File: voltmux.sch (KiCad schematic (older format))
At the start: 32 parts, among them J5 Conn_02x07_Odd_Even, U10 CD74HC4067SM

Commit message: Updated all the caps (I think) mostly changed to 0805
- Added 0603 footprints to new resistors which is slightly different from the old 0603 resistors for some reason???
- Annotated the schematic
- Still need to do the inductor oof
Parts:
- C13: footprint Capacitor_SMD:C_1206_3216Metric -> Capacitor_SMD:C_0805_2012Metric; Comment (none) -> 0.1µF -20%, +80% 16V Ceramic Capacitor Y5V 0805 (2012 Metri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; Digikey Number (none) -> 399-9159-2-ND; Part Number (none) -> C0805C104Z4VACTU; Price ($) (none) -> 0.11
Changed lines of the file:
@@
 	2350 3550 2350 3500
-$Comp
-L Device:C_Small C13
-U 1 1 5F5548EC
-P 2500 1250
-F 0 "C13" H 2592 1296 50  0000 L CNN
-F 1 "0.1uF" H 2592 1205 50  0000 L CNN
-F 2 "Capacitor_SMD:C_1206_3216Metric" H 2500 1250 50  0001 C CNN
-F 3 "~" H 2500 1250 50  0001 C CNN
-	1    2500 1250
-	1    0    0    -1
-$EndComp
 $Comp
 L power:GND #PWR046
@@
 	10450 2100 10400 2100
 NoConn ~ 10450 2700
+$Comp
+L Device:C_Small C?
+U 1 1 5FD72535
+P 2500 1250
+AR Path="/5FD72535" Ref="C?"  Part="1"
+AR Path="/5F70A721/5FD72535" Ref="C13"  Part="1"
+F 0 "C13" H 2592 1296 50  0000 L CNN
+F 1 "0.1uF" H 2592 1205 50  0000 L CNN
+F 2 "Capacitor_SMD:C_0805_2012Metric" H 2500 1250 50  0001 C CNN
+F 3 "https://content.kemet.com/datasheets/KEM_C1005_Y5V_SMD.pdf" H 2500 1250 50  0001 C CNN
+F 4 "C0805C104Z4VACTU" H 2500 1250 50  0001 C CNN "Part Number"
+F 5 "399-9159-2-ND" H 2500 1250 50  0001 C CNN "Digikey Number"
+F 6 "0.11" H 2500 1250 50  0001 C CNN "Price ($)"
+F 7 "0.1µF -20%, +80% 16V Ceramic Capacitor Y5V 0805 (2012 Metric)" H 2500 1250 50  0001 C CNN "Comment"
+	1    2500 1250
+	1    0    0    -1
+$EndComp
 $EndSCHEMATC

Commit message: Reset 0604 resistors to smaller (older?) footprint size
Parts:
- R31, R32, R33, R34, R35, R36, R37, R38, R39, R40, R41, R42, R43, R44, R45, R46, R47, R48, R49, R50, R51, R52, R53, R54, R55, R56, R57, R58, R59: footprint Resistor_SMD:R_0603_1608Metric_Pad1.05x0.95mm_HandSolder -> Resistor_SMD:R_0603_1608Metric_Pad0.98x0.95mm_HandSolder
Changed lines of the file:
@@
 F 0 "R31" H 5370 1696 50  0000 L CNN
 F 1 "360k" H 5370 1605 50  0000 L CNN
-F 2 "Resistor_SMD:R_0603_1608Metric_Pad1.05x0.95mm_HandSolder" V 5230 1650 50  0001 C CNN
+F 2 "Resistor_SMD:R_0603_1608Metric_Pad0.98x0.95mm_HandSolder" V 5230 1650 50  0001 C CNN
 F 3 "~" H 5300 1650 50  0001 C CNN
 	1    5300 1650
@@
 F 0 "R37" H 5370 2196 50  0000 L CNN
 F 1 "360k" H 5370 2105 50  0000 L CNN
-F 2 "Resistor_SMD:R_0603_1608Metric_Pad1.05x0.95mm_HandSolder" V 5230 2150 50  0001 C CNN
+F 2 "Resistor_SMD:R_0603_1608Metric_Pad0.98x0.95mm_HandSolder" V 5230 2150 50  0001 C CNN
 F 3 "~" H 5300 2150 50  0001 C CNN
 	1    5300 2150
@@
 F 0 "R32" H 5970 1696 50  0000 L CNN
 F 1 "200k" H 5970 1605 50  0000 L CNN
-F 2 "Resistor_SMD:R_0603_1608Metric_Pad1.05x0.95mm_HandSolder" V 5830 1650 50  0001 C CNN
+F 2 "Resistor_SMD:R_0603_1608Metric_Pad0.98x0.95mm_HandSolder" V 5830 1650 50  0001 C CNN
 F 3 "~" H 5900 1650 50  0001 C CNN
 	1    5900 1650
@@
 F 0 "R38" H 5970 2196 50  0000 L CNN
 F 1 "100k" H 5970 2105 50  0000 L CNN
-F 2 "Resistor_SMD:R_0603_1608Metric_Pad1.05x0.95mm_HandSolder" V 5830 2150 50  0001 C CNN
+F 2 "Resistor_SMD:R_0603_1608Metric_Pad0.98x0.95mm_HandSolder" V 5830 2150 50  0001 C CNN
 F 3 "~" H 5900 2150 50  0001 C CNN
 	1    5900 2150
@@
 F 0 "R33" H 6570 1696 50  0000 L CNN
 F 1 "330k" H 6570 1605 50  0000 L CNN
-F 2 "Resistor_SMD:R_0603_1608Metric_Pad1.05x0.95mm_HandSolder" V 6430 1650 50  0001 C CNN
+F 2 "Resistor_SMD:R_0603_1608Metric_Pad0.98x0.95mm_HandSolder" V 6430 1650 50  0001 C CNN
 F 3 "~" H 6500 1650 50  0001 C CNN
 	1    6500 1650
@@
 F 0 "R39" H 6570 2196 50  0000 L CNN
 F 1 "100k" H 6570 2105 50  0000 L CNN
-F 2 "Resistor_SMD:R_0603_1608Metric_Pad1.05x0.95mm_HandSolder" V 6430 2150 50  0001 C CNN
+F 2 "Resistor_SMD:R_0603_1608Metric_Pad0.98x0.95mm_HandSolder" V 6430 2150 50  0001 C CNN
 F 3 "~" H 6500 2150 50  0001 C CNN
 	1    6500 2150
@@
 F 0 "R34" H 7170 1696 50  0000 L CNN
 F 1 "500k" H 7170 1605 50  0000 L CNN
-F 2 "Resistor_SMD:R_0603_1608Metric_Pad1.05x0.95mm_HandSolder" V 7030 1650 50  0001 C CNN
+F 2 "Resistor_SMD:R_0603_1608Metric_Pad0.98x0.95mm_HandSolder" V 7030 1650 50  0001 C CNN
 F 3 "~" H 7100 1650 50  0001 C CNN
 	1    7100 1650
@@
 F 0 "R40" H 7170 2196 50  0000 L CNN
 F 1 "100k" H 7170 2105 50  0000 L CNN
-F 2 "Resistor_SMD:R_0603_1608Metric_Pad1.05x0.95mm_HandSolder" V 7030 2150 50  0001 C CNN
+F 2 "Resistor_SMD:R_0603_1608Metric_Pad0.98x0.95mm_HandSolder" V 7030 2150 50  0001 C CNN
 F 3 "~" H 7100 2150 50  0001 C CNN
 	1    7100 2150
@@
 F 0 "R35" H 7770 1696 50  0000 L CNN
 F 1 "500k" H 7770 1605 50  0000 L CNN
-F 2 "Resistor_SMD:R_0603_1608Metric_Pad1.05x0.95mm_HandSolder" V 7630 1650 50  0001 C CNN
+F 2 "Resistor_SMD:R_0603_1608Metric_Pad0.98x0.95mm_HandSolder" V 7630 1650 50  0001 C CNN
 F 3 "~" H 7700 1650 50  0001 C CNN
 	1    7700 1650
@@
 F 0 "R41" H 7770 2196 50  0000 L CNN
 F 1 "100k" H 7770 2105 50  0000 L CNN
-F 2 "Resistor_SMD:R_0603_1608Metric_Pad1.05x0.95mm_HandSolder" V 7630 2150 50  0001 C CNN
+F 2 "Resistor_SMD:R_0603_1608Metric_Pad0.98x0.95mm_HandSolder" V 7630 2150 50  0001 C CNN
 F 3 "~" H 7700 2150 50  0001 C CNN
 	1    7700 2150
@@
 F 0 "R36" H 8370 1696 50  0000 L CNN
 F 1 "560k" H 8370 1605 50  0000 L CNN
-F 2 "Resistor_SMD:R_0603_1608Metric_Pad1.05x0.95mm_HandSolder" V 8230 1650 50  0001 C CNN
+F 2 "Resistor_SMD:R_0603_1608Metric_Pad0.98x0.95mm_HandSolder" V 8230 1650 50  0001 C CNN
 F 3 "~" H 8300 1650 50  0001 C CNN
 	1    8300 1650
@@
 F 0 "R42" H 8370 2196 50  0000 L CNN
 F 1 "47k" H 8370 2105 50  0000 L CNN
-F 2 "Resistor_SMD:R_0603_1608Metric_Pad1.05x0.95mm_HandSolder" V 8230 2150 50  0001 C CNN
+F 2 "Resistor_SMD:R_0603_1608Metric_Pad0.98x0.95mm_HandSolder" V 8230 2150 50  0001 C CNN
 F 3 "~" H 8300 2150 50  0001 C CNN
 	1    8300 2150
@@
 F 0 "R45" H 5520 3296 50  0000 L CNN
 F 1 "560k" H 5520 3205 50  0000 L CNN
-F 2 "Resistor_SMD:R_0603_1608Metric_Pad1.05x0.95mm_HandSolder" V 5380 3250 50  0001 C CNN
+F 2 "Resistor_SMD:R_0603_1608Metric_Pad0.98x0.95mm_HandSolder" V 5380 3250 50  0001 C CNN
 F 3 "~" H 5450 3250 50  0001 C CNN
 	1    5450 3250
@@
 F 0 "R51" H 5520 3796 50  0000 L CNN
 F 1 "39.2k" H 5520 3705 50  0000 L CNN
-F 2 "Resistor_SMD:R_0603_1608Metric_Pad1.05x0.95mm_HandSolder" V 5380 3750 50  0001 C CNN
+F 2 "Resistor_SMD:R_0603_1608Metric_Pad0.98x0.95mm_HandSolder" V 5380 3750 50  0001 C CNN
 F 3 "~" H 5450 3750 50  0001 C CNN
 	1    5450 3750
@@
 F 0 "R46" H 6220 3296 50  0000 L CNN
 F 1 "500k" H 6220 3205 50  0000 L CNN
-F 2 "Resistor_SMD:R_0603_1608Metric_Pad1.05x0.95mm_HandSolder" V 6080 3250 50  0001 C CNN
+F 2 "Resistor_SMD:R_0603_1608Metric_Pad0.98x0.95mm_HandSolder" V 6080 3250 50  0001 C CNN
 F 3 "~" H 6150 3250 50  0001 C CNN
 	1    6150 3250
@@
 F 0 "R52" H 6220 3796 50  0000 L CNN
 F 1 "30k" H 6220 3705 50  0000 L CNN
-F 2 "Resistor_SMD:R_0603_1608Metric_Pad1.05x0.95mm_HandSolder" V 6080 3750 50  0001 C CNN
+F 2 "Resistor_SMD:R_0603_1608Metric_Pad0.98x0.95mm_HandSolder" V 6080 3750 50  0001 C CNN
 F 3 "~" H 6150 3750 50  0001 C CNN
 	1    6150 3750
@@
 F 0 "R47" H 6920 3296 50  0000 L CNN
 F 1 "560k" H 6920 3205 50  0000 L CNN
-F 2 "Resistor_SMD:R_0603_1608Metric_Pad1.05x0.95mm_HandSolder" V 6780 3250 50  0001 C CNN
+F 2 "Resistor_SMD:R_0603_1608Metric_Pad0.98x0.95mm_HandSolder" V 6780 3250 50  0001 C CNN
 F 3 "~" H 6850 3250 50  0001 C CNN
 	1    6850 3250
@@
 F 0 "R53" H 6920 3796 50  0000 L CNN
 F 1 "30k" H 6920 3705 50  0000 L CNN
-F 2 "Resistor_SMD:R_0603_1608Metric_Pad1.05x0.95mm_HandSolder" V 6780 3750 50  0001 C CNN
+F 2 "Resistor_SMD:R_0603_1608Metric_Pad0.98x0.95mm_HandSolder" V 6780 3750 50  0001 C CNN
 F 3 "~" H 6850 3750 50  0001 C CNN
 	1    6850 3750
@@
 F 0 "R48" H 7620 3296 50  0000 L CNN
 F 1 "330k" H 7620 3205 50  0000 L CNN
-F 2 "Resistor_SMD:R_0603_1608Metric_Pad1.05x0.95mm_HandSolder" V 7480 3250 50  0001 C CNN
+F 2 "Resistor_SMD:R_0603_1608Metric_Pad0.98x0.95mm_HandSolder" V 7480 3250 50  0001 C CNN
 F 3 "~" H 7550 3250 50  0001 C CNN
 	1    7550 3250
@@
 F 0 "R59" H 7620 4246 50  0000 L CNN
 F 1 "47.5k" H 7620 4155 50  0000 L CNN
-F 2 "Resistor_SMD:R_0603_1608Metric_Pad1.05x0.95mm_HandSolder" V 7480 4200 50  0001 C CNN
+F 2 "Resistor_SMD:R_0603_1608Metric_Pad0.98x0.95mm_HandSolder" V 7480 4200 50  0001 C CNN
 F 3 "~" H 7550 4200 50  0001 C CNN
 	1    7550 4200
@@
 F 0 "R49" H 8320 3296 50  0000 L CNN
 F 1 "500k" H 8320 3205 50  0000 L CNN
-F 2 "Resistor_SMD:R_0603_1608Metric_Pad1.05x0.95mm_HandSolder" V 8180 3250 50  0001 C CNN
+F 2 "Resistor_SMD:R_0603_1608Metric_Pad0.98x0.95mm_HandSolder" V 8180 3250 50  0001 C CNN
 F 3 "~" H 8250 3250 50  0001 C CNN
 	1    8250 3250
@@
 F 0 "R54" H 8320 3796 50  0000 L CNN
 F 1 "30k" H 8320 3705 50  0000 L CNN
-F 2 "Resistor_SMD:R_0603_1608Metric_Pad1.05x0.95mm_HandSolder" V 8180 3750 50  0001 C CNN
+F 2 "Resistor_SMD:R_0603_1608Metric_Pad0.98x0.95mm_HandSolder" V 8180 3750 50  0001 C CNN
 F 3 "~" H 8250 3750 50  0001 C CNN
 	1    8250 3750
@@
 F 0 "R43" H 6950 2500 50  0000 L CNN
 F 1 "25k" H 6900 2400 50  0000 L CNN
-F 2 "Resistor_SMD:R_0603_1608Metric_Pad1.05x0.95mm_HandSolder" V 7030 2450 50  0001 C CNN
+F 2 "Resistor_SMD:R_0603_1608Metric_Pad0.98x0.95mm_HandSolder" V 7030 2450 50  0001 C CNN
 F 3 "~" H 7100 2450 50  0001 C CNN
 	1    7100 2450
@@
 F 0 "R44" H 8150 2500 50  0000 L CNN
 F 1 "47k" H 8100 2400 50  0000 L CNN
-F 2 "Resistor_SMD:R_0603_1608Metric_Pad1.05x0.95mm_HandSolder" V 8230 2450 50  0001 C CNN
+F 2 "Resistor_SMD:R_0603_1608Metric_Pad0.98x0.95mm_HandSolder" V 8230 2450 50  0001 C CNN
 F 3 "~" H 8300 2450 50  0001 C CNN
 	1    8300 2450
@@
 F 0 "R55" H 5300 4100 50  0000 L CNN
 F 1 "39.2k" H 5200 4000 50  0000 L CNN
-F 2 "Resistor_SMD:R_0603_1608Metric_Pad1.05x0.95mm_HandSolder" V 5380 4050 50  0001 C CNN
+F 2 "Resistor_SMD:R_0603_1608Metric_Pad0.98x0.95mm_HandSolder" V 5380 4050 50  0001 C CNN
 F 3 "~" H 5450 4050 50  0001 C CNN
 	1    5450 4050
@@
 F 0 "R56" H 6000 4100 50  0000 L CNN
 F 1 "33.2k" H 5950 4000 50  0000 L CNN
-F 2 "Resistor_SMD:R_0603_1608Metric_Pad1.05x0.95mm_HandSolder" V 6080 4050 50  0001 C CNN
+F 2 "Resistor_SMD:R_0603_1608Metric_Pad0.98x0.95mm_HandSolder" V 6080 4050 50  0001 C CNN
 F 3 "~" H 6150 4050 50  0001 C CNN
 	1    6150 4050
@@
 F 0 "R57" H 6700 4100 50  0000 L CNN
 F 1 "33.2k" H 6600 4000 50  0000 L CNN
-F 2 "Resistor_SMD:R_0603_1608Metric_Pad1.05x0.95mm_HandSolder" V 6780 4050 50  0001 C CNN
+F 2 "Resistor_SMD:R_0603_1608Metric_Pad0.98x0.95mm_HandSolder" V 6780 4050 50  0001 C CNN
 F 3 "~" H 6850 4050 50  0001 C CNN
 	1    6850 4050
@@
 F 0 "R50" H 7400 3600 50  0000 L CNN
 F 1 "147k" H 7300 3500 50  0000 L CNN
-F 2 "Resistor_SMD:R_0603_1608Metric_Pad1.05x0.95mm_HandSolder" V 7480 3550 50  0001 C CNN
+F 2 "Resistor_SMD:R_0603_1608Metric_Pad0.98x0.95mm_HandSolder" V 7480 3550 50  0001 C CNN
 F 3 "~" H 7550 3550 50  0001 C CNN
 	1    7550 3550
@@
 F 0 "R58" H 8320 4096 50  0000 L CNN
 F 1 "16.2k" H 8320 4005 50  0000 L CNN
-F 2 "Resistor_SMD:R_0603_1608Metric_Pad1.05x0.95mm_HandSolder" V 8180 4050 50  0001 C CNN
+F 2 "Resistor_SMD:R_0603_1608Metric_Pad0.98x0.95mm_HandSolder" V 8180 4050 50  0001 C CNN
 F 3 "~" H 8250 4050 50  0001 C CNN
 	1    8250 4050

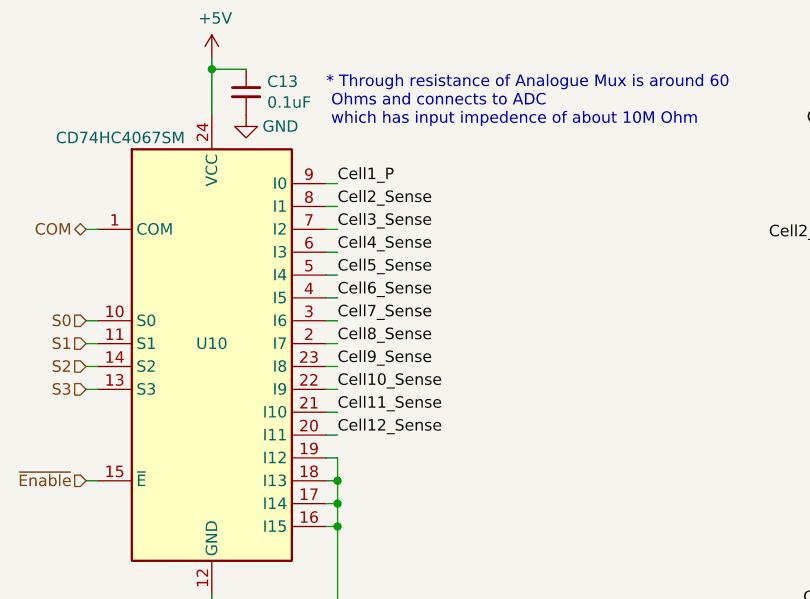
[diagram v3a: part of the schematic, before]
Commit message: Finish PCB Layout Preliminary
- Moved around temp connections to the analogue mux to help aid layout
- Moved around voltage sense connections too
- Moved around LED status shift reg
- " and the 7 seg shift reg
- Added filled copper layers
- Removed external ADC Input
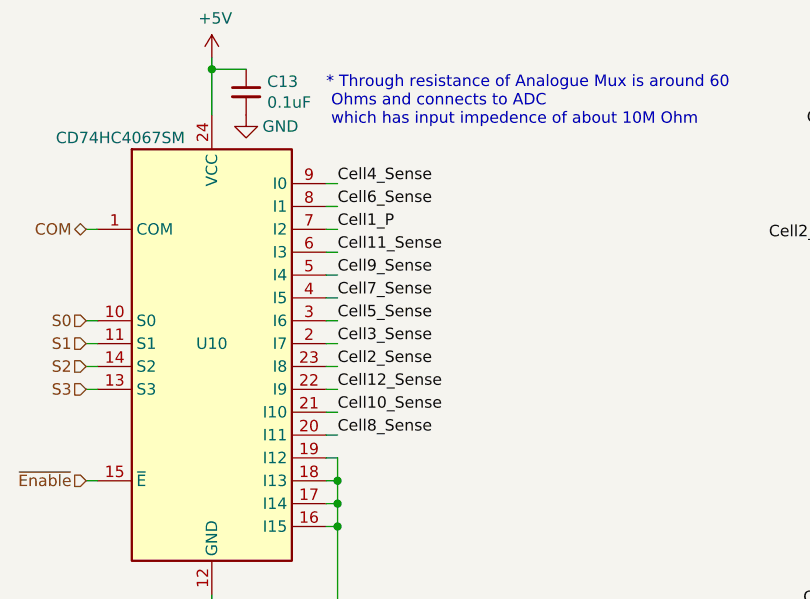
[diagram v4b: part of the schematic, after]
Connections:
- net Cell10_Sense: now also U10.21 (I10); no longer U10.22 (I9)
- net Cell11_Sense: now also U10.6 (I3); no longer U10.21 (I10)
- net Cell12_Sense: now also U10.22 (I9); no longer U10.20 (I11)
- net Cell1_P: now also U10.7 (I2); no longer U10.9 (I0)
- net Cell2_Sense: now also U10.23 (I8); no longer U10.8 (I1)
- net Cell3_Sense: now also U10.2 (I7); no longer U10.7 (I2)
- net Cell4_Sense: now also U10.9 (I0); no longer U10.6 (I3)
- net Cell5_Sense: now also U10.3 (I6); no longer U10.5 (I4)
- net Cell6_Sense: now also U10.8 (I1); no longer U10.4 (I5)
- net Cell7_Sense: now also U10.4 (I5); no longer U10.3 (I6)
- net Cell8_Sense: now also U10.20 (I11); no longer U10.2 (I7)
- net Cell9_Sense: now also U10.5 (I4); no longer U10.23 (I8)
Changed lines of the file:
@@
 Wire Wire Line
 	10450 2200 10400 2200
-Text Label 2900 1650 0    50   ~ 0
+Text Label 2900 1850 0    50   ~ 0
 Cell1_P
 Wire Wire Line
@@
 	1    0    0    -1
 $EndComp
+Text Label 2900 2450 0    50   ~ 0
+Cell2_Sense
+Text Label 2900 2350 0    50   ~ 0
+Cell3_Sense
+Text Label 2900 1650 0    50   ~ 0
+Cell4_Sense
+Text Label 2900 2250 0    50   ~ 0
+Cell5_Sense
 Text Label 2900 1750 0    50   ~ 0
-Cell2_Sense
-Text Label 2900 1850 0    50   ~ 0
-Cell3_Sense
+Cell6_Sense
+Text Label 2900 2150 0    50   ~ 0
+Cell7_Sense
+Text Label 2900 2750 0    50   ~ 0
+Cell8_Sense
+Text Label 2900 2050 0    50   ~ 0
+Cell9_Sense
+Text Label 2900 2650 0    50   ~ 0
+Cell10_Sense
 Text Label 2900 1950 0    50   ~ 0
-Cell4_Sense
-Text Label 2900 2050 0    50   ~ 0
-Cell5_Sense
-Text Label 2900 2150 0    50   ~ 0
-Cell6_Sense
-Text Label 2900 2250 0    50   ~ 0
-Cell7_Sense
-Text Label 2900 2350 0    50   ~ 0
-Cell8_Sense
-Text Label 2900 2450 0    50   ~ 0
-Cell9_Sense
+Cell11_Sense
 Text Label 2900 2550 0    50   ~ 0
-Cell10_Sense
-Text Label 2900 2650 0    50   ~ 0
-Cell11_Sense
-Text Label 2900 2750 0    50   ~ 0
 Cell12_Sense
 Wire Wire Line

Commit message: Updated some properties and generated BOM with KiBOM
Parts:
- J5: Comment (none) -> Connector Header Surface Mount 14 position 0.079\" (2.00mm); Digikey Number (none) -> WM6815TR-ND; Part Number (none) -> 0878325623; Price ($) (none) -> 1.56
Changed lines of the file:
@@
 F 1 "Conn_02x07_Odd_Even" H 10150 2826 50  0000 C CNN
 F 2 "uBMS-2:Molex_Milli_Grid_0878325623_TopBottom" H 10100 2400 50  0001 C CNN
-F 3 "~" H 10100 2400 50  0001 C CNN
+F 3 "https://media.digikey.com/pdf/Data%20Sheets/Molex%20PDFs/87832-300_Pkg_Spec.pdf" H 10100 2400 50  0001 C CNN
+F 4 "0878325623" H 10100 2400 50  0001 C CNN "Part Number"
+F 5 "WM6815TR-ND" H 10100 2400 50  0001 C CNN "Digikey Number"
+F 6 "1.56" H 10100 2400 50  0001 C CNN "Price ($)"
+F 7 "Connector Header Surface Mount 14 position 0.079\" (2.00mm)" H 10100 2400 50  0001 C CNN "Comment"
 	1    10100 2400
 	1    0    0    -1

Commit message: Added more part info
- also updated BOM
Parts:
- U10: Comment (none) -> 1 Circuit IC Switch 16:1 160Ohm 24-SSOP; Digikey Number (none) -> 296-9226-2-ND; Part Number (none) -> CD74HC4067SM96; Price ($) (none) -> 0.79
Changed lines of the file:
@@
 F 2 "Package_SO:SSOP-24_5.3x8.2mm_P0.65mm" H 3400 1350 50  0001 C CIN
 F 3 "http://www.ti.com/lit/ds/symlink/cd74hc4067.pdf" H 2000 3200 50  0001 C CNN
+F 4 "CD74HC4067SM96" H 2350 2350 50  0001 C CNN "Part Number"
+F 5 "296-9226-2-ND" H 2350 2350 50  0001 C CNN "Digikey Number"
+F 6 "0.79" H 2350 2350 50  0001 C CNN "Price ($)"
+F 7 "1 Circuit IC Switch 16:1 160Ohm 24-SSOP" H 2350 2350 50  0001 C CNN "Comment"
 	1    2350 2350
 	1    0    0    -1
